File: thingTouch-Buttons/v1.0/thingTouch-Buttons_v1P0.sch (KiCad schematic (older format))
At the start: 23 parts, among them P1 DIRECT_CONN, P2 TOUCH_CONN, U1 TTP224N-BSB

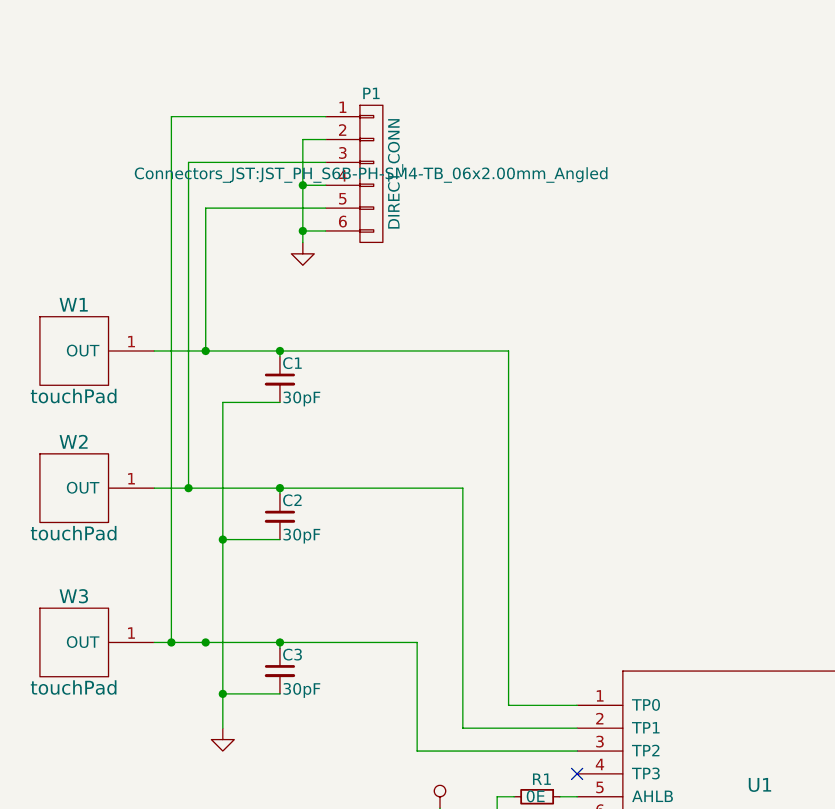
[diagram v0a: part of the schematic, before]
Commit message: following changes are done
Layout following changes done
-> 2.0mm mounting holes added
-> company logo and name
-> fab details
-> rerouting of touch signals and VDD signals
-> Bom created
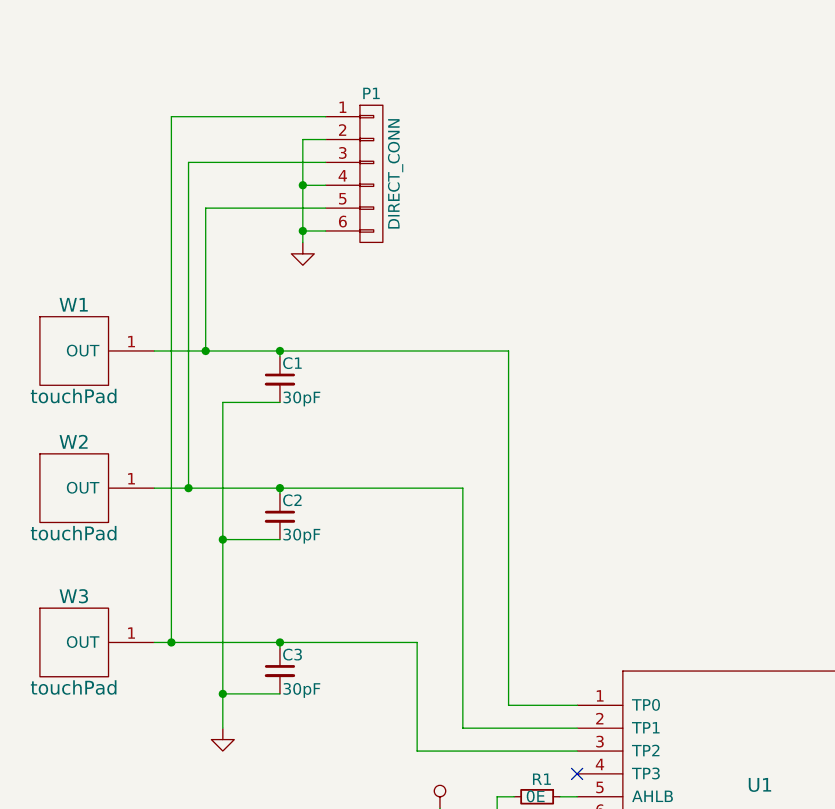
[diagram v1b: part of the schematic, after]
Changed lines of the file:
@@
 LIBS:contrib
 LIBS:valves
-LIBS:touchpad_single
-LIBS:ttp224n-bsb
 LIBS:thingTouch-Buttons_v1P0-cache
 EELAYER 25 0
@@
 	2475 4200 2475 3725
 Connection ~ 1875 3725
-Connection ~ 1550 3725
 Connection ~ 1475 3050
 Wire Wire Line
@@
 F 0 "P1" H 2275 2025 50  0000 C CNN
 F 1 "DIRECT_CONN" V 2375 1675 50  0000 C CNN
-F 2 "Connectors_JST:JST_PH_S6B-PH-SM4-TB_06x2.00mm_Angled" H 2275 1675 50  0000 C CNN
+F 2 "Connectors_JST:JST_PH_S6B-PH-SM4-TB_06x2.00mm_Angled" H 2275 1675 50  0001 C CNN
 F 3 "" H 2275 1675 50  0000 C CNN
 	1    2275 1675

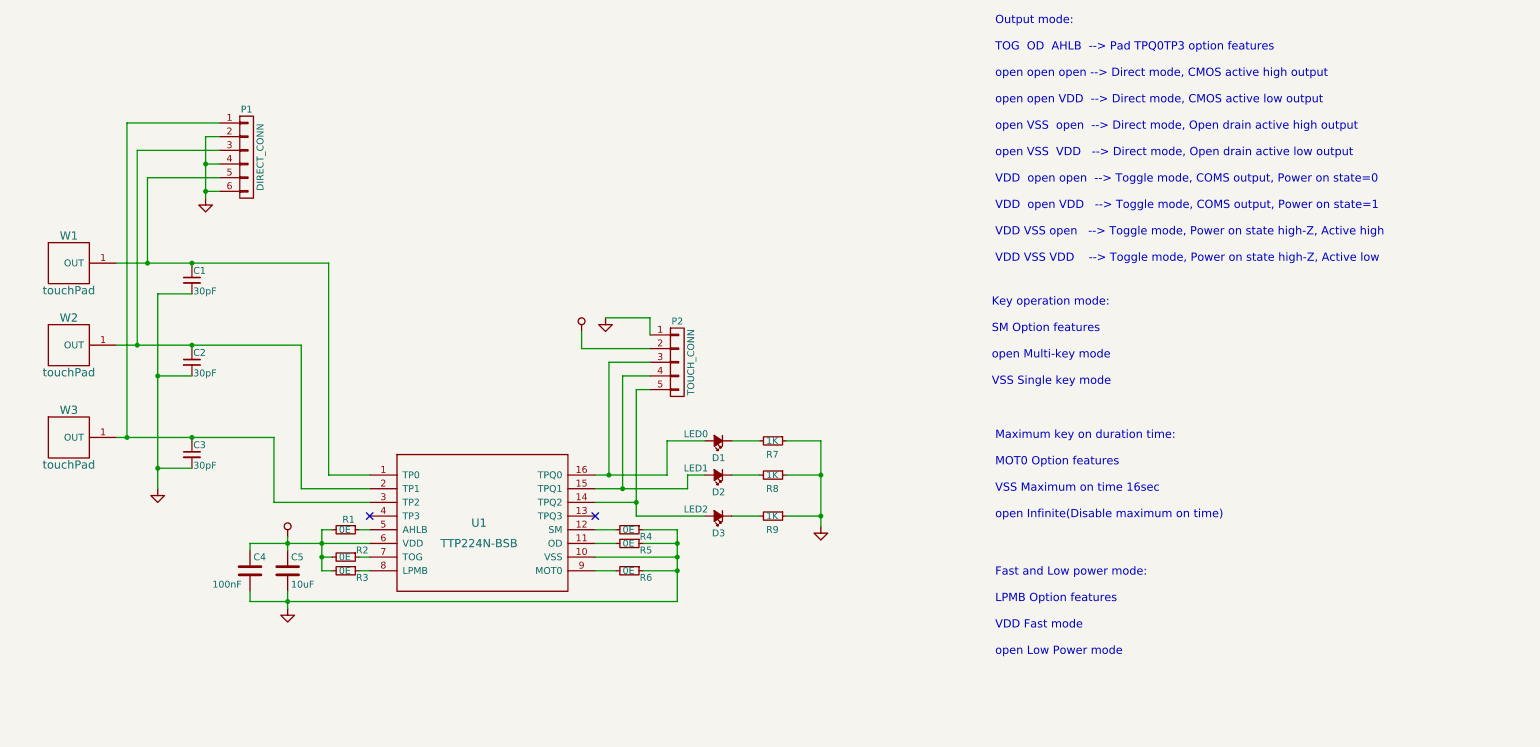
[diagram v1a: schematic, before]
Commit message: in schematic transistor switching,side leds added right angle connector s added
in schematic transistor switching logic, side leds added ,right angle
connector s added
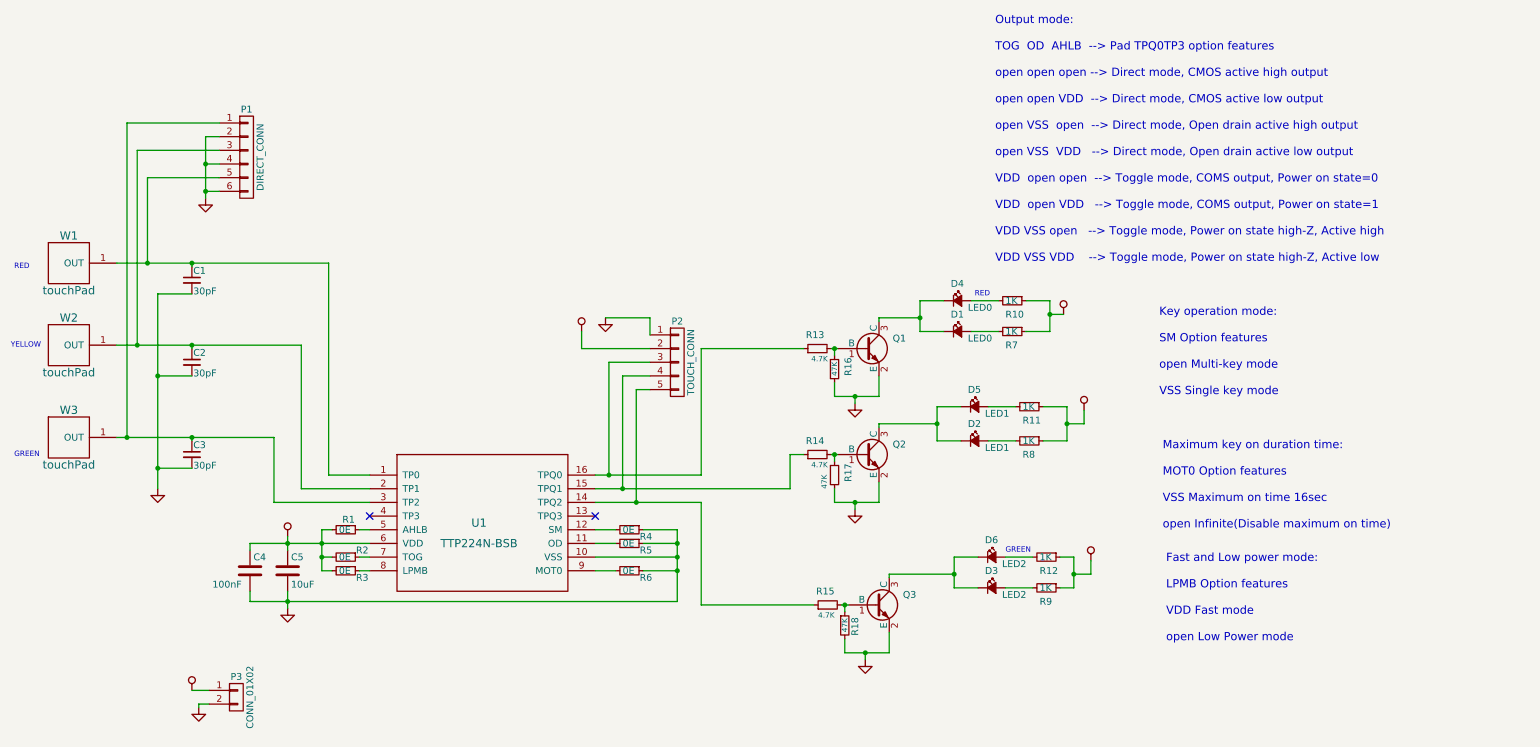
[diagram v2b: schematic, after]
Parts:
- removed U1: TTP224N-BSB, Housings_SSOP:SSOP-16_3.9x4.9mm_Pitch0.635mm, symbol TTP224N-BSB-RESCUE-thingTouch-Buttons_v1P0
- added D4: LED0, SIM_MODULES:LED_0805_Side_led, symbol Led_Small
- added D5: LED1, SIM_MODULES:LED_0805_Side_led, symbol Led_Small
- added D6: LED2, SIM_MODULES:LED_0805_Side_led, symbol Led_Small
- added P3: CONN_01X02, Connectors_JST:JST_EH_S02B-EH_02x2.50mm_Angled, symbol CONN_01X02
- added Q1, Q2, Q3: MMBT3904, TO_SOT_Packages_SMD:SOT-23, symbol MMBT3904
- added R10, R11, R12: 1K, Resistors_SMD:R_0805_HandSoldering, symbol R_Small
- added R13, R14, R15: 4.7K, Resistors_SMD:R_0805_HandSoldering, symbol R_Small
- added R16, R17, R18: 47K, Resistors_SMD:R_0805_HandSoldering, symbol R_Small
- added U1: TTP224N-BSB, Housings_SSOP:SSOP-16_3.9x4.9mm_Pitch0.635mm, symbol TTP224N-BSB
- D1, D2, D3: footprint LEDs:LED_0805_HandSoldering -> SIM_MODULES:LED_0805_Side_led
- P1: footprint Connectors_JST:JST_PH_S6B-PH-SM4-TB_06x2.00mm_Angled -> Connectors_JST:JST_EH_S06B-EH_06x2.50mm_Angled
- P2: footprint Connectors_JST:JST_PH_S5B-PH-SM4-TB_05x2.00mm_Angled -> Connectors_JST:JST_EH_S06B-EH_06x2.50mm_Angled
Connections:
- net GND: now also P3.2 (P2), Q1.2 (E), Q2.2 (E), Q3.2 (E), R16.2, R17.2, R18.2, U1.10 (VSS); no longer R7.1, R8.1, R9.1
- net VDD: now also R7.1, R8.1, R9.1, P3.1 (P1), R10.1, R11.1, R12.1, U1.6 (VDD)
- net at C1.1, P1.5 (P5), W1.1 (OUT): now also U1.1 (TP0)
- net at C2.1, P1.3 (P3), W2.1 (OUT): now also U1.2 (TP1)
- net at C3.1, P1.1 (P1), W3.1 (OUT): now also U1.3 (TP2)
- net at R5.2: now also U1.11 (OD)
- net at R4.2: now also U1.12 (SM)
- net at P2.5 (P5): now also R15.1, U1.14 (TPQ2); no longer D3.2 (A)
- net at P2.4 (P4): now also R14.1, U1.15 (TPQ1); no longer D2.2 (A)
- net at P2.3 (P3): now also R13.1, U1.16 (TPQ0); no longer D1.2 (A)
- net at R1.1: now also U1.5 (AHLB)
- net at R2.1: now also U1.7 (TOG)
- net at R3.1: now also U1.8 (LPMB)
- net at R6.2: now also U1.9 (MOT0)
- net at D2.1 (K): now also D5.1 (K), Q2.3 (C); no longer R8.2
- net at D1.1 (K): now also D4.1 (K), Q1.3 (C); no longer R7.2
- net at D3.1 (K): now also D6.1 (K), Q3.3 (C); no longer R9.2
- new net: D2.2 (A), R8.2
- new net: D1.2 (A), R7.2
- new net: D3.2 (A), R9.2
- new net: D4.2 (A), R10.2
- new net: D5.2 (A), R11.2
- new net: D6.2 (A), R12.2
- new net: Q1.1 (B), R13.2, R16.1
- new net: Q2.1 (B), R14.2, R17.1
- new net: Q3.1 (B), R15.2, R18.1
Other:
- note added: "GREEN"
- note added: "RED"
- note added: "YELLOW"
- moved on the sheet: D1, D2, D3, R7, R8, R9

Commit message: verified the layout
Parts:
- P3: value CONN_01X02 -> POWER_CONN
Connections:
- net at P2.3 (P3), U1.16 (TPQ0): now also R15.1; no longer R13.1
- net at P2.5 (P5), U1.14 (TPQ2): now also R13.1; no longer R15.1
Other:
- moved on the sheet: D1, D3, D4, D6, Q1, Q3, R10, R12, R13, R15, R16, R18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

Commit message: merged pull request
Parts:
- U1: symbol TTP224N-BSB -> TTP224N-BSB-RESCUE-thingTouch-Buttons_v1P0
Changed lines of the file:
@@
 EESchema Schematic File Version 2
+LIBS:thingTouch-Buttons_v1P0-rescue
 LIBS:power
 LIBS:device
@@
 Connection ~ 1975 1725
 $Comp
-L TTP224N-BSB U1
+L TTP224N-BSB-RESCUE-thingTouch-Buttons_v1P0 U1
 U 1 1 596F6FAA
 P 3975 4350

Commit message: Gerbers generated, design verified
Gerbers generated, design verified
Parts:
- removed P2: TOUCH_CONN, Connectors_JST:JST_EH_S06B-EH_06x2.50mm_Angled, symbol CONN_01X05
- added P2: TOUCH_CONN, Connectors_JST:JST_EH_S06B-EH_06x2.50mm_Angled, symbol CONN_01X06
- U1: symbol TTP224N-BSB-RESCUE-thingTouch-Buttons_v1P0 -> TTP224N-BSB
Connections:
- net GND: now also P2.2 (P2), P2.6 (P6); no longer P1.4 (P4)
- net VDD: now also P1.1 (P1), P2.1 (P1)
- net at C2.1, U1.2 (TP1), W2.1 (OUT): now also P1.4 (P4); no longer P1.3 (P3)
- net at C3.1, U1.3 (TP2), W3.1 (OUT): now also P1.3 (P3); no longer P1.1 (P1)
- net at R15.1, U1.16 (TPQ0): now also P2.5 (P5)
- net at R14.1, U1.15 (TPQ1): now also P2.4 (P4)
- net at R13.1, U1.14 (TPQ2): now also P2.3 (P3)
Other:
- moved on the sheet: P1
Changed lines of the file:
@@
 EESchema Schematic File Version 2
-LIBS:thingTouch-Buttons_v1P0-rescue
 LIBS:power
 LIBS:device
@@
 LIBS:contrib
 LIBS:valves
-LIBS:ttp224n-bsb
-LIBS:touchpad_single
 LIBS:thingTouch-Buttons_v1P0-cache
 EELAYER 25 0
@@
 L GND #PWR02
 U 1 1 596D1262
-P 1975 1975
-F 0 "#PWR02" H 1975 2025 30  0001 C CNN
-F 1 "GND" H 1975 1850 30  0001 C CNN
-F 2 "" H 1975 1975 60  0000 C CNN
-F 3 "" H 1975 1975 60  0000 C CNN
-	1    1975 1975
+P 1725 2075
+F 0 "#PWR02" H 1725 2125 30  0001 C CNN
+F 1 "GND" H 1725 1950 30  0001 C CNN
+F 2 "" H 1725 2075 60  0000 C CNN
+F 3 "" H 1725 2075 60  0000 C CNN
+	1    1725 2075
 	1    0    0    -1
 $EndComp
@@
 L GND #PWR05
 U 1 1 596D455F
-P 4900 2850
-F 0 "#PWR05" H 4900 2900 30  0001 C CNN
-F 1 "GND" H 4900 2725 30  0001 C CNN
-F 2 "" H 4900 2850 60  0000 C CNN
-F 3 "" H 4900 2850 60  0000 C CNN
-	1    4900 2850
+P 4725 3075
+F 0 "#PWR05" H 4725 3125 30  0001 C CNN
+F 1 "GND" H 4725 2950 30  0001 C CNN
+F 2 "" H 4725 3075 60  0000 C CNN
+F 3 "" H 4725 3075 60  0000 C CNN
+	1    4725 3075
 	1    0    0    -1
 $EndComp
@@
 L VDD #PWR06
 U 1 1 596D4D6D
-P 4725 2950
-F 0 "#PWR06" H 4725 3175 30  0001 C CNN
-F 1 "VDD" V 4675 2950 30  0001 C CNN
-F 2 "" H 4625 2700 60  0001 C CNN
-F 3 "" H 4725 2800 60  0001 C CNN
-	1    4725 2950
+P 5050 2975
+F 0 "#PWR06" H 5050 3200 30  0001 C CNN
+F 1 "VDD" V 5000 2975 30  0001 C CNN
+F 2 "" H 4950 2725 60  0001 C CNN
+F 3 "" H 5050 2825 60  0001 C CNN
+	1    5050 2975
 	1    0    0    -1
 $EndComp
 NoConn ~ 4825 4300
-$Comp
-L CONN_01X05 P2
-U 1 1 596D66CB
-P 5425 3175
-F 0 "P2" H 5425 3475 50  0000 C CNN
-F 1 "TOUCH_CONN" V 5525 3175 50  0000 C CNN
-F 2 "Connectors_JST:JST_EH_S06B-EH_06x2.50mm_Angled" H 5425 3175 50  0001 C CNN
-F 3 "" H 5425 3175 50  0000 C CNN
-	1    5425 3175
-	1    0    0    -1
-$EndComp
 $Comp
 L Led_Small D2
@@
 Connection ~ 5425 4500
 Wire Wire Line
-	4900 2850 5225 2850
-Wire Wire Line
-	5225 2850 5225 2975
-Wire Wire Line
-	4725 2950 4725 3075
-Wire Wire Line
 	4725 3075 5225 3075
-Wire Wire Line
-	4925 3175 5225 3175
-Wire Wire Line
-	5125 3375 5225 3375
-Wire Wire Line
-	5025 3275 5225 3275
 Wire Wire Line
 	7325 3750 7500 3750
@@
 	7825 2950 8025 2950
 Connection ~ 5025 4100
-Wire Wire Line
-	1550 1825 1550 2450
 Connection ~ 1550 2450
-Wire Wire Line
-	1475 1625 1475 3050
-Wire Wire Line
-	1400 1425 1400 3725
-Connection ~ 1400 3725
-Wire Wire Line
-	4925 3175 4925 4000
 Connection ~ 4925 4000
 Connection ~ 5125 4200
@@
 L CONN_01X06 P1
 U 1 1 596DD16E
-P 2275 1675
-F 0 "P1" H 2275 2025 50  0000 C CNN
-F 1 "DIRECT_CONN" V 2375 1675 50  0000 C CNN
-F 2 "Connectors_JST:JST_EH_S06B-EH_06x2.50mm_Angled" H 2275 1675 50  0001 C CNN
-F 3 "" H 2275 1675 50  0000 C CNN
-	1    2275 1675
-	1    0    0    -1
-$EndComp
-Wire Wire Line
-	1400 1425 2075 1425
-Wire Wire Line
-	1475 1625 2075 1625
-Wire Wire Line
-	2075 1825 1550 1825
-Wire Wire Line
-	2075 1925 1975 1925
-Wire Wire Line
-	1975 1525 1975 1975
-Wire Wire Line
-	2075 1725 1975 1725
-Connection ~ 1975 1925
-Wire Wire Line
-	2075 1525 1975 1525
-Connection ~ 1975 1725
-$Comp
-L TTP224N-BSB-RESCUE-thingTouch-Buttons_v1P0 U1
+P 2025 1775
+F 0 "P1" H 2025 2125 50  0000 C CNN
+F 1 "DIRECT_CONN" V 2125 1775 50  0000 C CNN
+F 2 "Connectors_JST:JST_EH_S06B-EH_06x2.50mm_Angled" H 2025 1775 50  0001 C CNN
+F 3 "" H 2025 1775 50  0000 C CNN
+	1    2025 1775
+	1    0    0    -1
+$EndComp
+$Comp
+L TTP224N-BSB U1
 U 1 1 596F6FAA
 P 3975 4350
@@
 	6900 3625 7325 3625
 Connection ~ 7325 3625
-Wire Wire Line
-	5125 4200 5125 3375
 Wire Wire Line
 	6975 2850 7450 2850
@@
 	4825 4100 6250 4100
 Wire Wire Line
-	5025 4100 5025 3275
-Wire Wire Line
 	6250 4100 6250 3850
 Wire Wire Line
@@
 	8450 2850 8325 2850
 Connection ~ 8325 2850
+Text Notes 7700 3425 0    59   ~ 0
+YELLOW
+$Comp
+L CONN_01X06 P2
+U 1 1 597F21C5
+P 5425 3225
+F 0 "P2" H 5425 3575 50  0000 C CNN
+F 1 "TOUCH_CONN" V 5525 3225 50  0000 C CNN
+F 2 "Connectors_JST:JST_EH_S06B-EH_06x2.50mm_Angled" H 5425 3225 50  0001 C CNN
+F 3 "" H 5425 3225 50  0000 C CNN
+	1    5425 3225
+	1    0    0    -1
+$EndComp
+Wire Wire Line
+	5050 2975 5225 2975
+Text Notes 5200 4000 0    59   ~ 0
+RED
+Text Notes 5200 4100 0    59   ~ 0
+YELLOW
+Text Notes 5200 4200 0    59   ~ 0
+GREEN
+Wire Wire Line
+	5225 3175 5125 3175
+Wire Wire Line
+	5125 3175 5125 4200
+Wire Wire Line
+	5225 3275 5025 3275
+Wire Wire Line
+	5025 3275 5025 4100
+Wire Wire Line
+	4925 4000 4925 3375
+Wire Wire Line
+	4925 3375 5225 3375
+$Comp
+L GND #PWR013
+U 1 1 597FAC5F
+P 5225 3550
+F 0 "#PWR013" H 5225 3600 30  0001 C CNN
+F 1 "GND" H 5225 3425 30  0001 C CNN
+F 2 "" H 5225 3550 60  0000 C CNN
+F 3 "" H 5225 3550 60  0000 C CNN
+	1    5225 3550
+	1    0    0    -1
+$EndComp
+Wire Wire Line
+	5225 3475 5225 3550
+Wire Wire Line
+	1925 5675 1925 5700
+Wire Wire Line
+	2000 5675 1925 5675
+$Comp
+L GND #PWR014
+U 1 1 5977631B
+P 1925 5700
+F 0 "#PWR014" H 1925 5750 30  0001 C CNN
+F 1 "GND" H 1925 5575 30  0001 C CNN
+F 2 "" H 1925 5700 60  0000 C CNN
+F 3 "" H 1925 5700 60  0000 C CNN
+	1    1925 5700
+	1    0    0    -1
+$EndComp
+Wire Wire Line
+	1875 5575 2000 5575
+$Comp
+L VDD #PWR015
+U 1 1 5977500B
+P 1875 5575
+F 0 "#PWR015" H 1875 5800 30  0001 C CNN
+F 1 "VDD" V 1825 5575 30  0001 C CNN
+F 2 "" H 1775 5325 60  0001 C CNN
+F 3 "" H 1875 5425 60  0001 C CNN
+	1    1875 5575
+	1    0    0    -1
+$EndComp
 $Comp
 L CONN_01X02 P3
@@
 $EndComp
 $Comp
-L VDD #PWR013
-U 1 1 5977500B
-P 1875 5575
-F 0 "#PWR013" H 1875 5800 30  0001 C CNN
-F 1 "VDD" V 1825 5575 30  0001 C CNN
-F 2 "" H 1775 5325 60  0001 C CNN
-F 3 "" H 1875 5425 60  0001 C CNN
-	1    1875 5575
-	1    0    0    -1
-$EndComp
-Wire Wire Line
-	1875 5575 2000 5575
-$Comp
-L GND #PWR014
-U 1 1 5977631B
-P 1925 5700
-F 0 "#PWR014" H 1925 5750 30  0001 C CNN
-F 1 "GND" H 1925 5575 30  0001 C CNN
-F 2 "" H 1925 5700 60  0000 C CNN
-F 3 "" H 1925 5700 60  0000 C CNN
-	1    1925 5700
-	1    0    0    -1
-$EndComp
-Wire Wire Line
-	2000 5675 1925 5675
-Wire Wire Line
-	1925 5675 1925 5700
-Text Notes 7700 3425 0    59   ~ 0
-YELLOW
+L VDD #PWR016
+U 1 1 597FFD10
+P 1650 1525
+F 0 "#PWR016" H 1650 1750 30  0001 C CNN
+F 1 "VDD" V 1600 1525 30  0001 C CNN
+F 2 "" H 1550 1275 60  0001 C CNN
+F 3 "" H 1650 1375 60  0001 C CNN
+	1    1650 1525
+	1    0    0    -1
+$EndComp
+Wire Wire Line
+	1650 1525 1825 1525
+$Comp
+L GND #PWR017
+U 1 1 59801CA5
+P 1425 1625
+F 0 "#PWR017" H 1425 1675 30  0001 C CNN
+F 1 "GND" H 1425 1500 30  0001 C CNN
+F 2 "" H 1425 1625 60  0000 C CNN
+F 3 "" H 1425 1625 60  0000 C CNN
+	1    1425 1625
+	1    0    0    -1
+$EndComp
+Wire Wire Line
+	1425 1625 1825 1625
+Wire Wire Line
+	1825 1725 1650 1725
+Wire Wire Line
+	1650 1725 1650 3200
+Wire Wire Line
+	1650 3200 1375 3200
+Wire Wire Line
+	1375 3200 1375 3725
+Connection ~ 1375 3725
+Wire Wire Line
+	1825 1825 1475 1825
+Wire Wire Line
+	1475 1825 1475 3050
+Wire Wire Line
+	1550 2450 1550 1925
+Wire Wire Line
+	1550 1925 1825 1925
+Wire Wire Line
+	1825 2025 1725 2025
+Wire Wire Line
+	1725 2025 1725 2075
 $EndSCHEMATC
